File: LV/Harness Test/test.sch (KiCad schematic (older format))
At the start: 14 parts

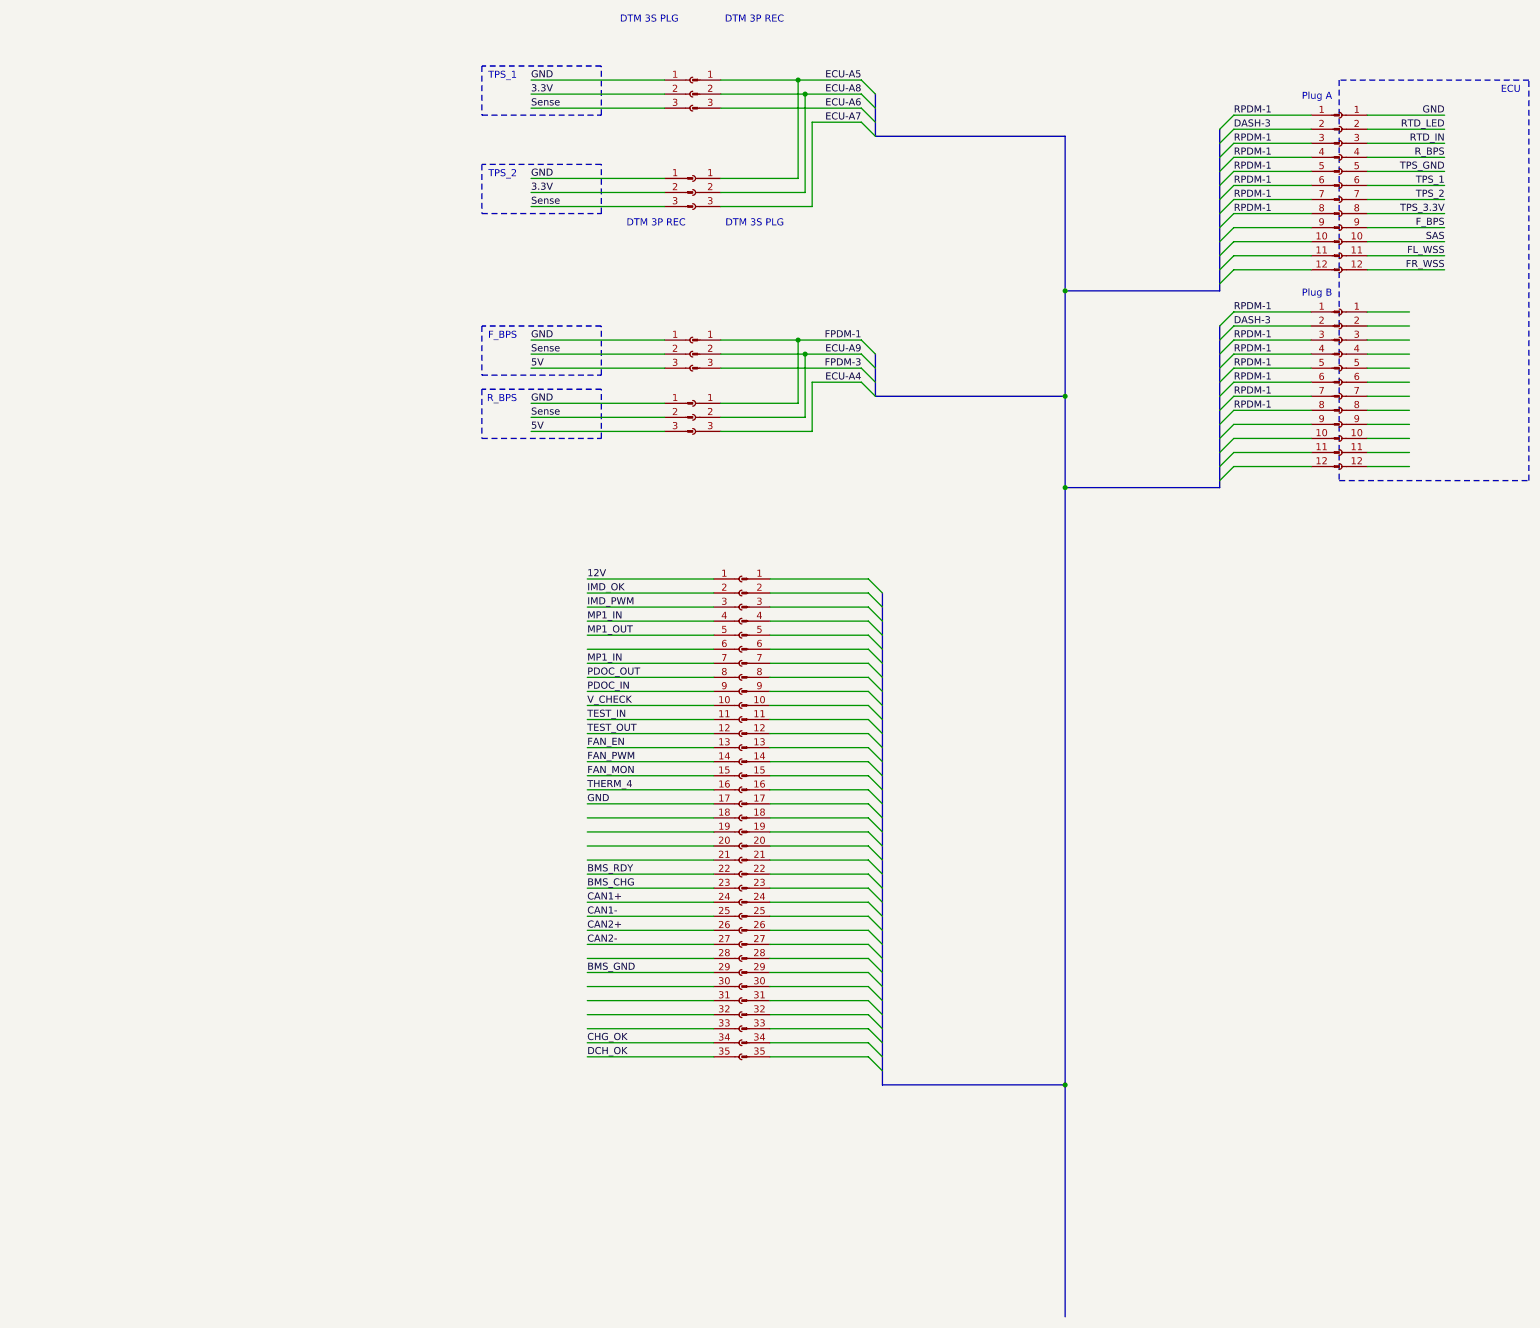
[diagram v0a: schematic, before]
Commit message: Added to LV Harness
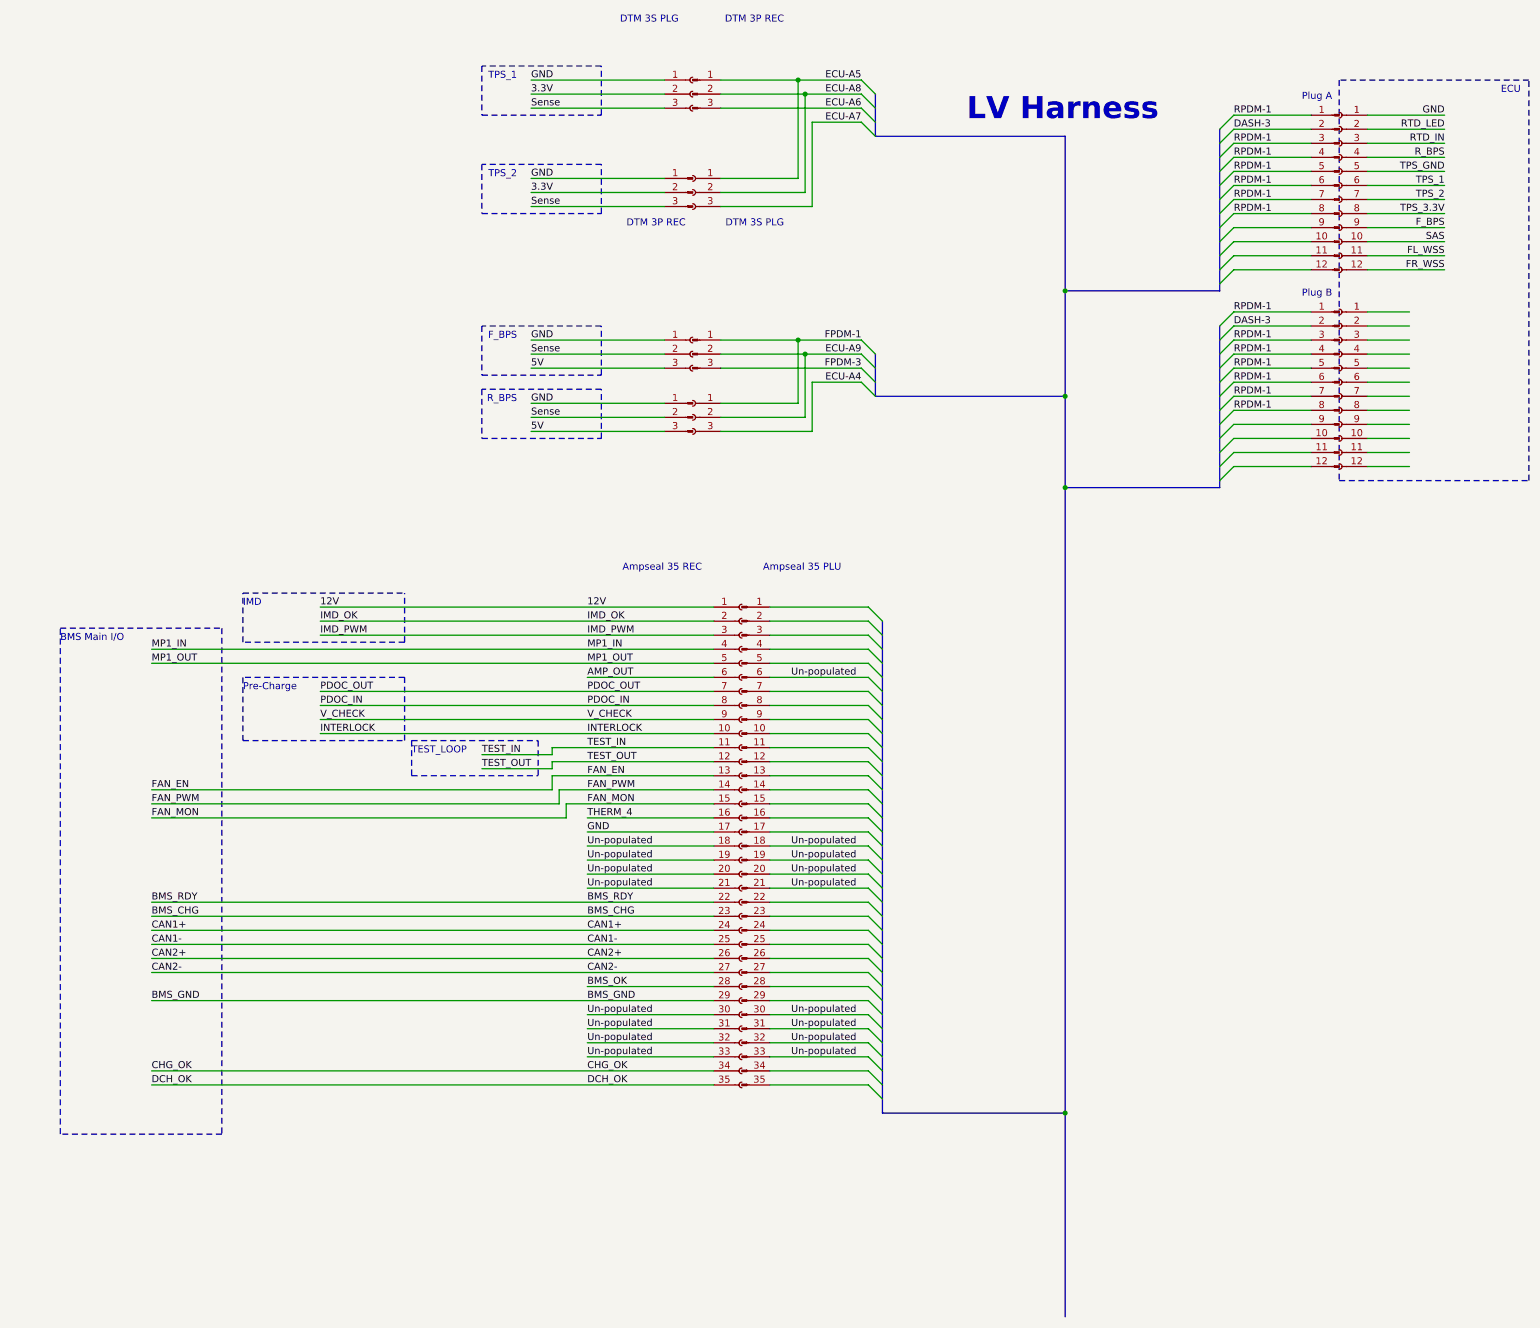
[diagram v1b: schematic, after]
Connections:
- net labels added: AMP_OUT, BMS_OK, INTERLOCK, Un-populated
- wire segments 154 -> 164
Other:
- note added: "Ampseal 35 PLU"
- note added: "Ampseal 35 REC"
- note added: "BMS Main I/O"
- note added: "IMD"
- note added: "LV Harness"
- note added: "Pre-Charge"
- note added: "TEST_LOOP"

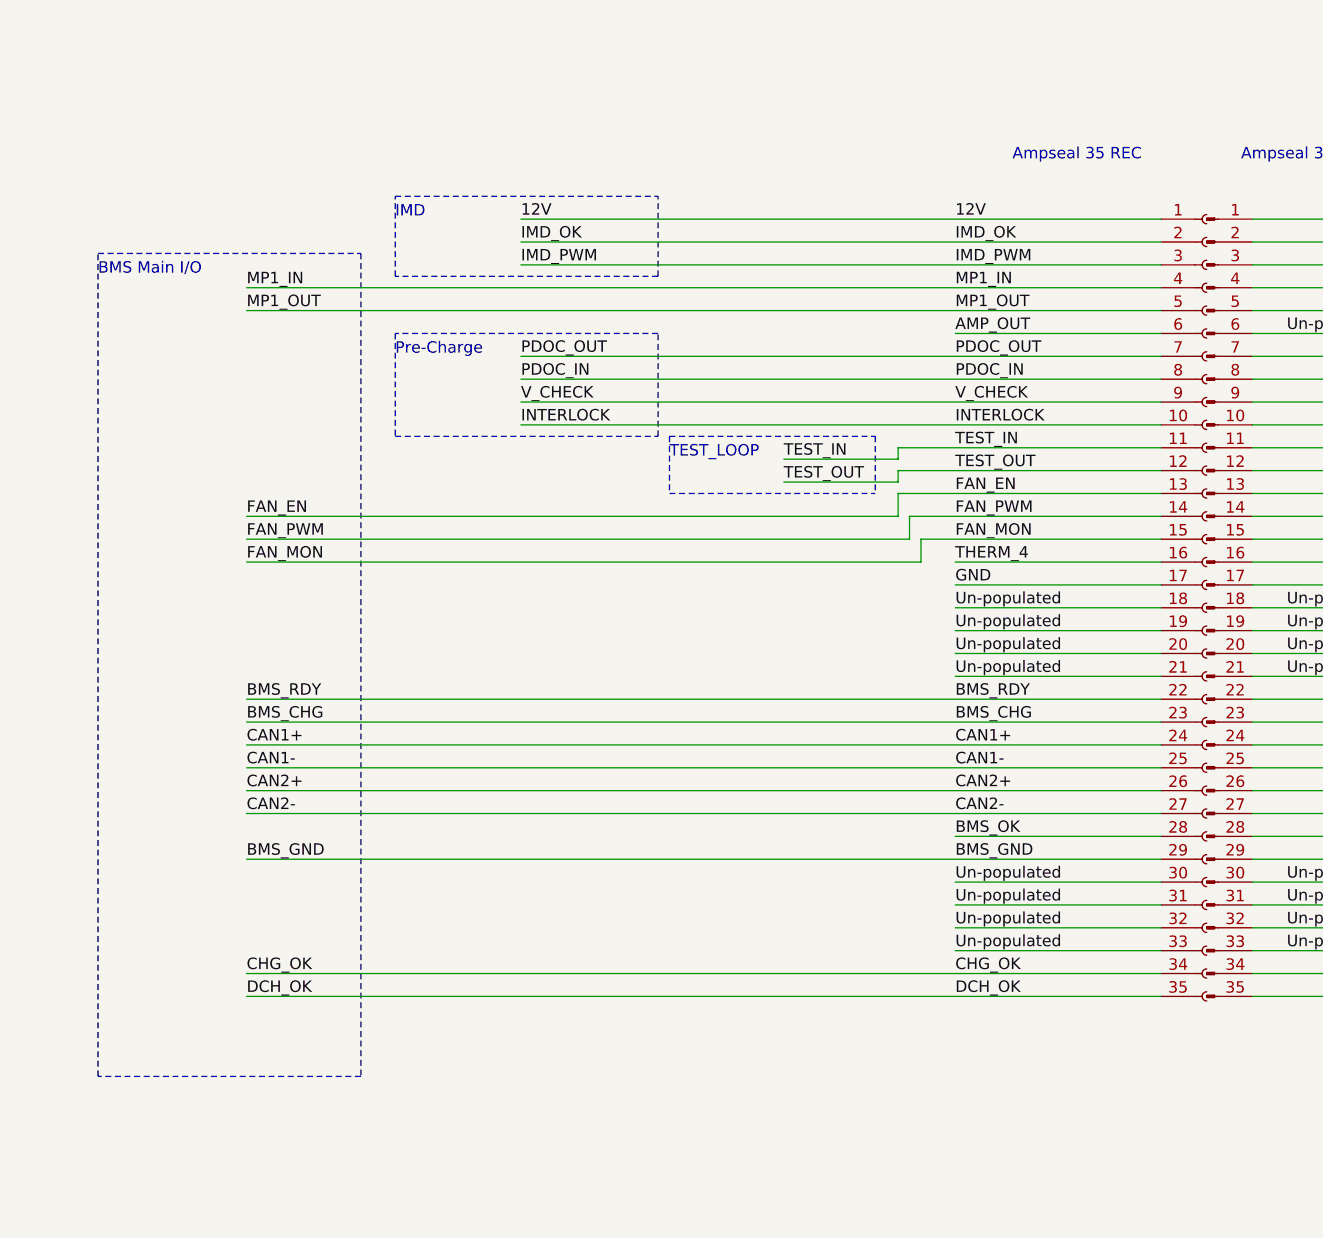
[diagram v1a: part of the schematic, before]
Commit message: Changes to LV Harness Schematic
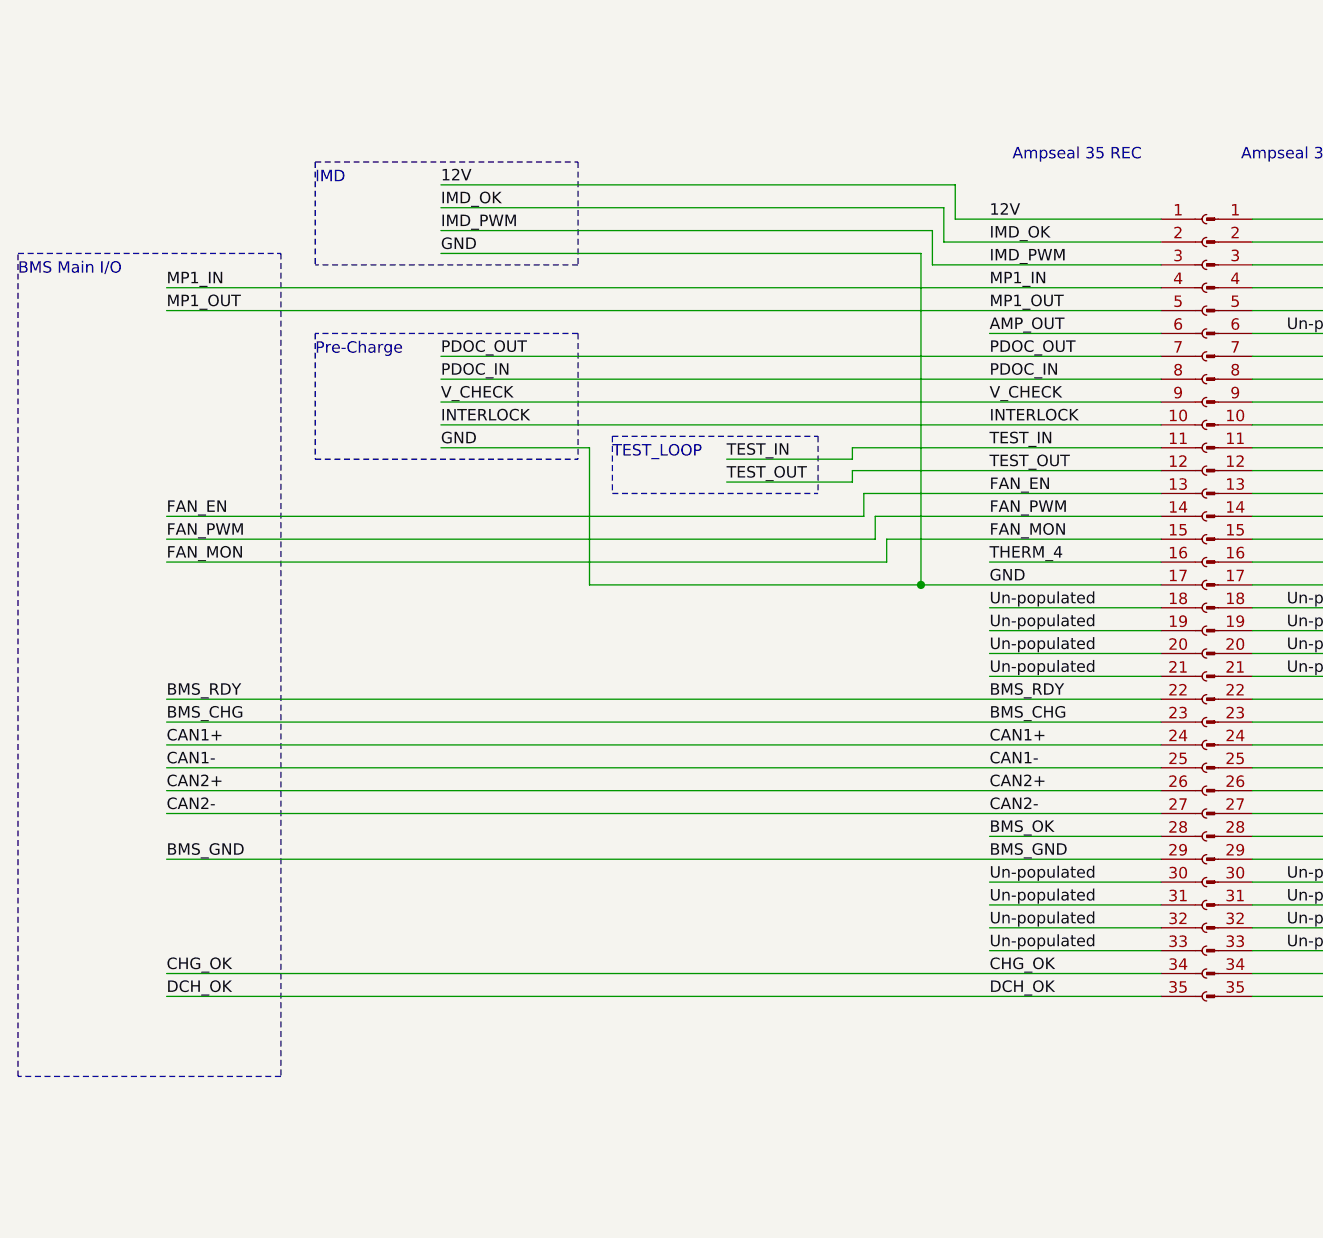
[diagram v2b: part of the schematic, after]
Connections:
- wire segments 164 -> 175
